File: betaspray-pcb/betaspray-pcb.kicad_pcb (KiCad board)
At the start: 2 copper layers, 99.3 x 99.3 mm, 44 parts, among them J10 Conn_01x09_Pin, J11 Conn_01x03_Pin, J12 Conn_01x03_Pin, J13 Conn_01x03_Pin, J14 Conn_01x03_Pin, J15 Conn_01x03_Pin, J16 Conn_01x03_Pin, J17 Conn_01x03_Pin, J18 Conn_01x03_Pin, J2 Conn_01x02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

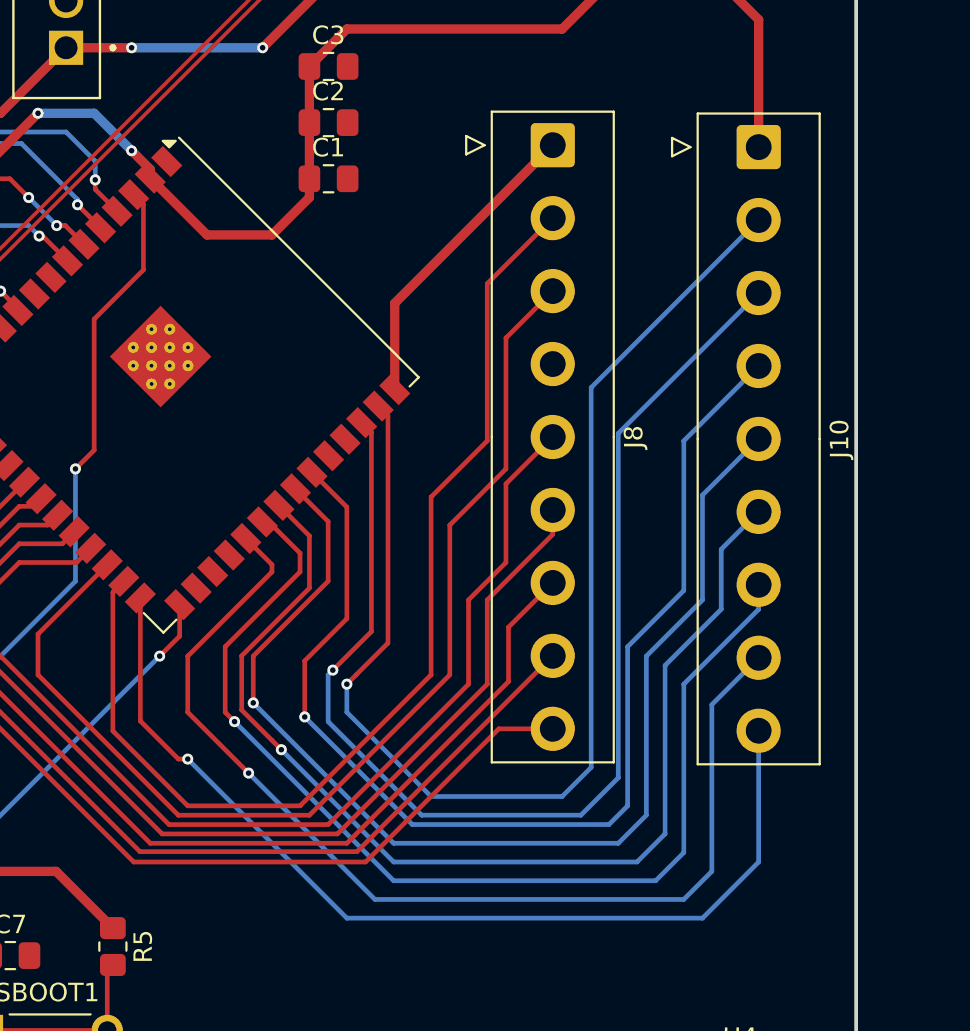
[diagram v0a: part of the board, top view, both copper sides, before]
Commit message: Fixed footprint
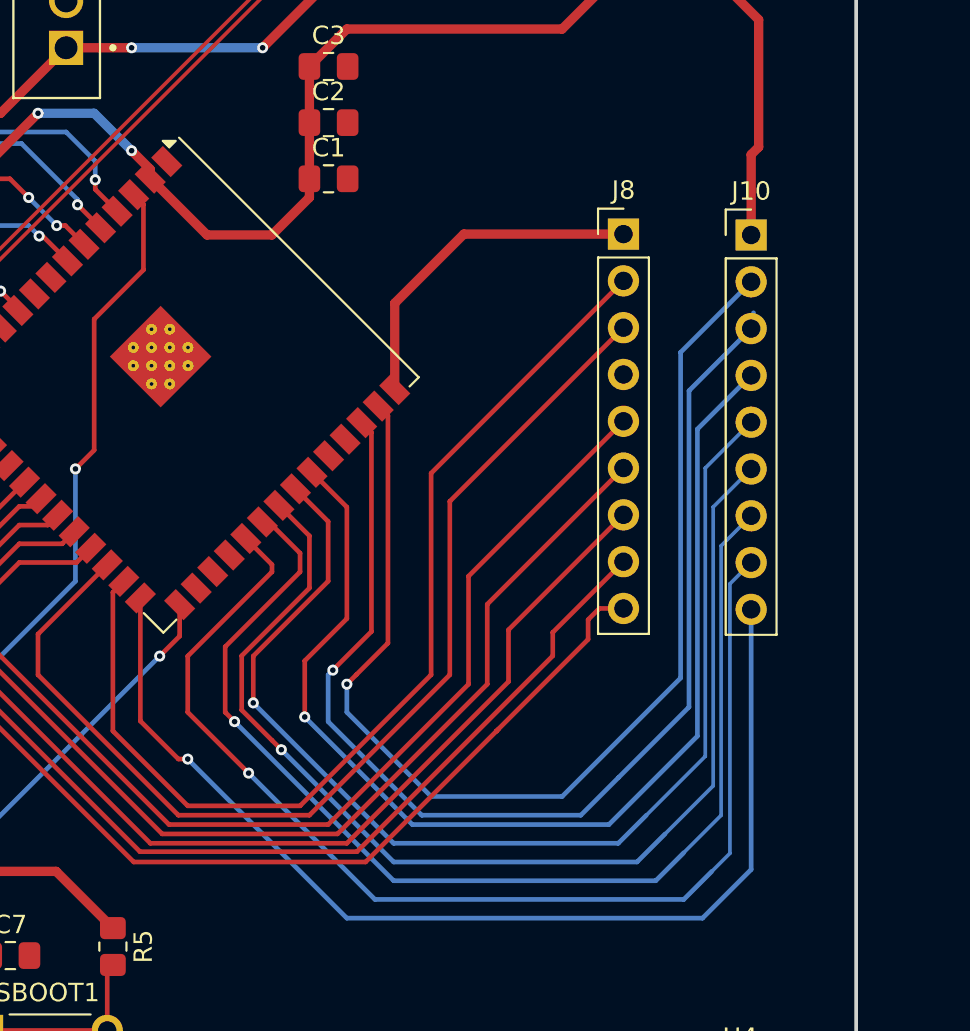
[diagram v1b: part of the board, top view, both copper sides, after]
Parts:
- J10, J8: footprint Connector_TE-Connectivity:TE_826576-9_1x09_P3.96mm_Vertical -> Connector_PinHeader_2.54mm:PinHeader_1x09_P2.54mm_Vertical
- moved J8 6.17 mm to (188.8, 74.6), turned to 0 degrees
- moved J10 4.79 mm to (195.7, 74.7), turned to 0 degrees
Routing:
- net CAM_PWR_DEL: track 54.5 -> 61.9 mm
- net D2: track 54.2 -> 61.0 mm
- net CAM_RST: track 53.1 -> 59.5 mm
- net D4: track 55.7 -> 61.0 mm
- net D3: track 57.8 -> 62.8 mm
- net VDD33: track 166.4 -> 171.4 mm
- net D6: track 57.1 -> 61.0 mm
- net D5: track 58.6 -> 62.2 mm
- net SCL: track 67.0 -> 63.5 mm
- net D8: track 58.6 -> 61.1 mm
- net D7: track 59.9 -> 62.1 mm
- net GND: track 47.8 -> 49.7 mm
- net SDA: track 57.8 -> 56.0 mm
- net VS_SYNC_FRAME: track 65.6 -> 64.4 mm
- net D9: track 62.1 -> 62.8 mm
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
